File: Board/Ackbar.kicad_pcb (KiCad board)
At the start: 2 copper layers, 101.6 x 50.8 mm, 15 parts, among them J1 TOF, J2 GNSS, J3 HALL, J4 MOTOR, J5 PWR_IN, J6 EPD, U1 ESP32-S3 Pico, U2 VREG, U3 TMC2209, U4 SN74LVC1G04

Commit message: Add pullup resistor to vreg enable
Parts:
- added R2: 1K, Resistor_SMD:R_0805_2012Metric_Pad1.20x1.40mm_HandSolder, F.Cu at (101.6, 53.6)
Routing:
- net /VIN: track 57.0 -> 64.2 mm
- net Net-(U2-EN): track 23.2 -> 30.2 mm
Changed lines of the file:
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@@
+    )
+  )
+  (footprint "Resistor_SMD:R_0805_2012Metric_Pad1.20x1.40mm_HandSolder" (layer "F.Cu")
+    (at 101.6 53.61 -90)
+    (descr "Resistor SMD 0805 (2012 Metric), square (rectangular) end terminal, IPC_7351 nominal with elongated pad for handsoldering. (Body size source: IPC-SM-782 page 72, https://www.pcb-3d.com/wordpress/wp-content/uploads/ipc-sm-782a_amendment_1_and_2.pdf), generated with kicad-footprint-generator")
+    (tags "resistor handsolder")
+    (property "Sheetfile" "Ackbar.kicad_sch")
+    (property "Sheetname" "")
+    (property "ki_description" "Resistor, US symbol")
+    (property "ki_keywords" "R res resistor")
+    (attr smd)
+    (fp_text reference "R2" (at 0 -1.65 90) (layer "F.SilkS")
+        (effects (font (size 1 1) (thickness 0.15)))
+    )
+    (fp_text value "1K" (at 0 1.65 90) (layer "F.Fab")
+        (effects (font (size 1 1) (thickness 0.15)))
+    )
+    (fp_text user "${REFERENCE}" (at 0 0 90) (layer "F.Fab")
+        (effects (font (size 0.5 0.5) (thickness 0.08)))
+    )
+    (fp_line (start -0.227064 -0.735) (end 0.227064 -0.735)
+      (stroke (width 0.12) (type solid)) (layer "F.SilkS"))
+    (fp_line (start -0.227064 0.735) (end 0.227064 0.735)
+      (stroke (width 0.12) (type solid)) (layer "F.SilkS"))
+    (fp_line (start -1.85 -0.95) (end 1.85 -0.95)
+      (stroke (width 0.05) (type solid)) (layer "F.CrtYd"))
+    (fp_line (start -1.85 0.95) (end -1.85 -0.95)
+      (stroke (width 0.05) (type solid)) (layer "F.CrtYd"))
+    (fp_line (start 1.85 -0.95) (end 1.85 0.95)
+      (stroke (width 0.05) (type solid)) (layer "F.CrtYd"))
+    (fp_line (start 1.85 0.95) (end -1.85 0.95)
+      (stroke (width 0.05) (type solid)) (layer "F.CrtYd"))
+    (fp_line (start -1 -0.625) (end 1 -0.625)
+      (stroke (width 0.1) (type solid)) (layer "F.Fab"))
+    (fp_line (start -1 0.625) (end -1 -0.625)
+      (stroke (width 0.1) (type solid)) (layer "F.Fab"))
+    (fp_line (start 1 -0.625) (end 1 0.625)
+      (stroke (width 0.1) (type solid)) (layer "F.Fab"))
+    (fp_line (start 1 0.625) (end -1 0.625)
+      (stroke (width 0.1) (type solid)) (layer "F.Fab"))
+    (pad "1" smd roundrect (at -1 0 270) (size 1.2 1.4) (layers "F.Cu" "F.Paste" "F.Mask") (roundrect_rratio 0.208333)
+      (net 11 "/VIN") (pintype "passive"))
+    (pad "2" smd roundrect (at 1 0 270) (size 1.2 1.4) (layers "F.Cu" "F.Paste" "F.Mask") (roundrect_rratio 0.208333)
+      (net 41 "Net-(U2-EN)") (pintype "passive"))
+    (model "${KICAD6_3DMODEL_DIR}/Resistor_SMD.3dshapes/R_0805_2012Metric.wrl"
+      (offset (xyz 0 0 0))
+      (scale (xyz 1 1 1))
+      (rotate (xyz 0 0 0))
     )
   )
@@
   (segment (start 69.85 52.385) (end 67.625 52.385) (width 0.5) (layer "F.Cu") (net 9))
   (via (at 67.31 52.07) (size 0.8) (drill 0.4) (layers "F.Cu" "B.Cu") (net 9))
+  (segment (start 101.6 52.61) (end 98.965 52.61) (width 0.5) (layer "F.Cu") (net 11))
+  (segment (start 98.425 52.07) (end 94.615 52.07) (width 0.5) (layer "F.Cu") (net 11))
+  (segment (start 98.965 52.61) (end 98.425 52.07) (width 0.5) (layer "F.Cu") (net 11))
   (segment (start 100.965 49.53) (end 100.965 43.815) (width 0.5) (layer "B.Cu") (net 11))
   (segment (start 76.878 29.253) (end 76.878 27.224334) (width 0.5) (layer "B.Cu") (net 11))
@@
   (segment (start 87.038 27.224334) (end 87.038 17.188) (width 0.5) (layer "B.Cu") (net 39))
   (segment (start 89.578 27.224334) (end 89.578 17.188) (width 0.5) (layer "B.Cu") (net 40))
+  (segment (start 94.615 54.61) (end 101.6 54.61) (width 0.25) (layer "F.Cu") (net 41))
   (segment (start 74.585 54.61) (end 94.615 54.61) (width 0.25) (layer "F.Cu") (net 41))
   (segment (start 72.36 52.385) (end 74.585 54.61) (width 0.25) (layer "F.Cu") (net 41))

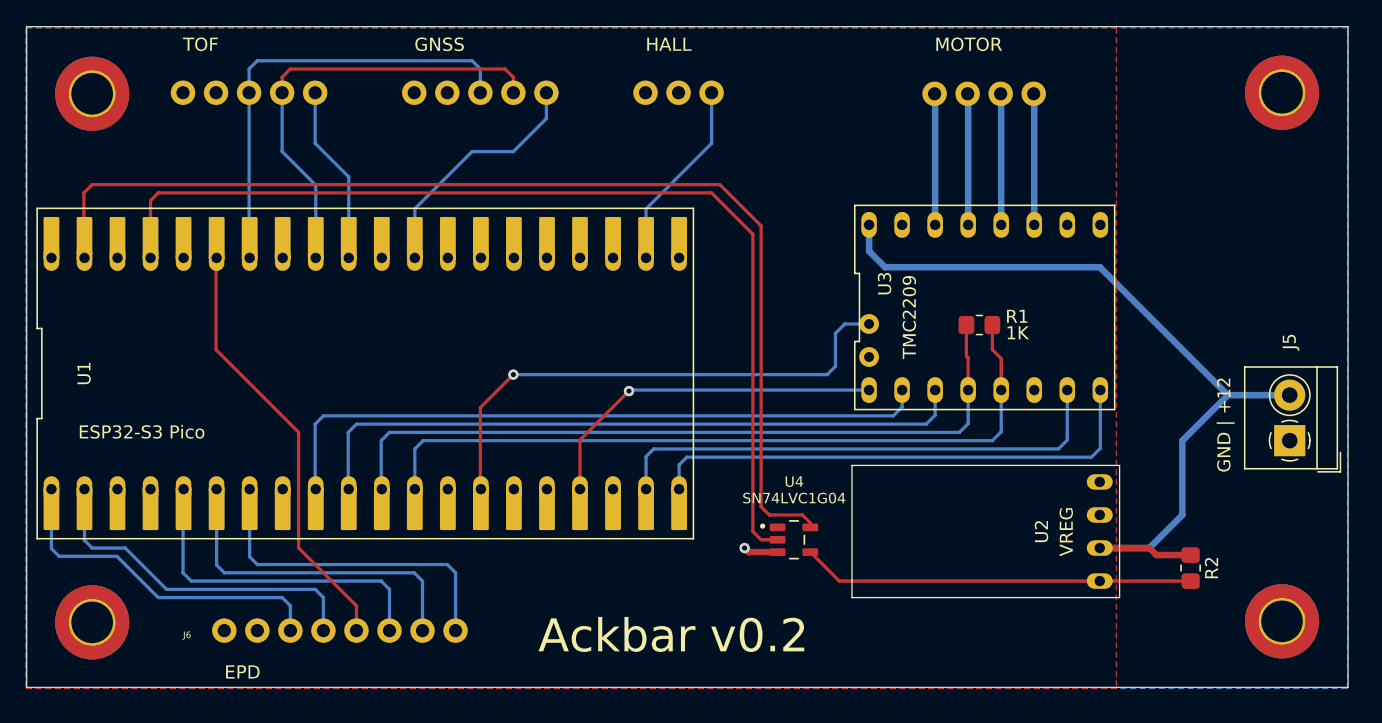
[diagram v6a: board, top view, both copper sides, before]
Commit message: Okay, you win, we're using the onboard regulator
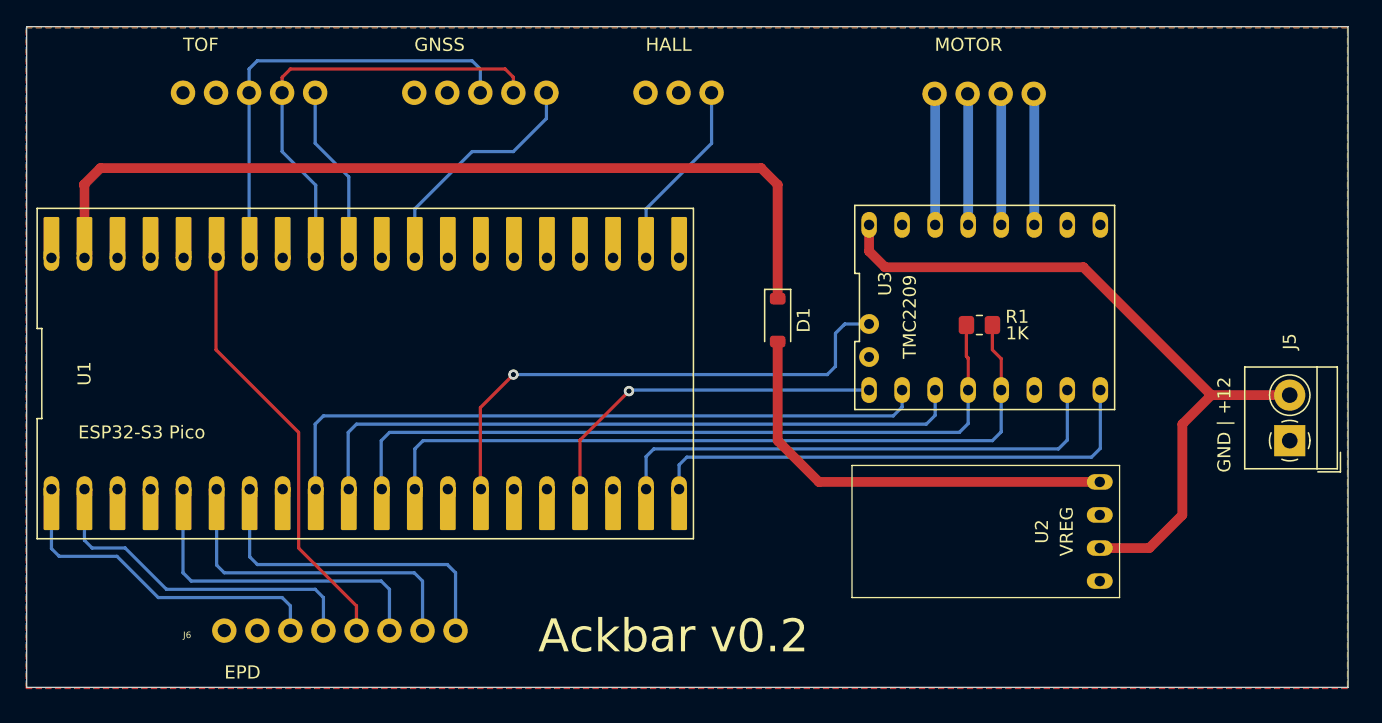
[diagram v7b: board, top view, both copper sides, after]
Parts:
- removed R2: 1K, Resistor_SMD:R_0805_2012Metric_Pad1.20x1.40mm_HandSolder
- removed REF** (x4): MountingHole_3.2mm_M3_ISO7380_Pad_TopBottom, MountingHole:MountingHole_3.2mm_M3_ISO7380_Pad_TopBottom
- removed U4: SN74LVC1G04, Ackbar:SOT95P280X145-5N
- added D1: MBR230LSFT1G, Diode_SMD:D_SOD-123, F.Cu at (69.8, 34.5)
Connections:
- U1 pad 37: Net-(U1-3V3_EN) -> unconnected-(U1-3V3_EN-Pad37)
- U1 pad 39: Net-(U1-VSYS) -> /VSYS
- U2 pad 1: /3V3 -> /VOUT
- U2 pad 4: Net-(U2-EN) -> unconnected-(U2-EN-Pad4)
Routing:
- net Net-(U1-VSYS): track 84.8 -> 0.00 mm
- net Net-(U1-3V3_EN): track 77.3 -> 0.00 mm
- net /VSYS: track 0.00 -> 68.8 mm
- net /VOUT: track 0.00 -> 33.7 mm
- net Net-(U2-EN): track 30.2 -> 0.00 mm
- net /VIN: track 64.2 -> 56.5 mm
- net /GND: track 2.67 -> 0.00 mm, vias 1 -> 0

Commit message: Replace missing mounting holes
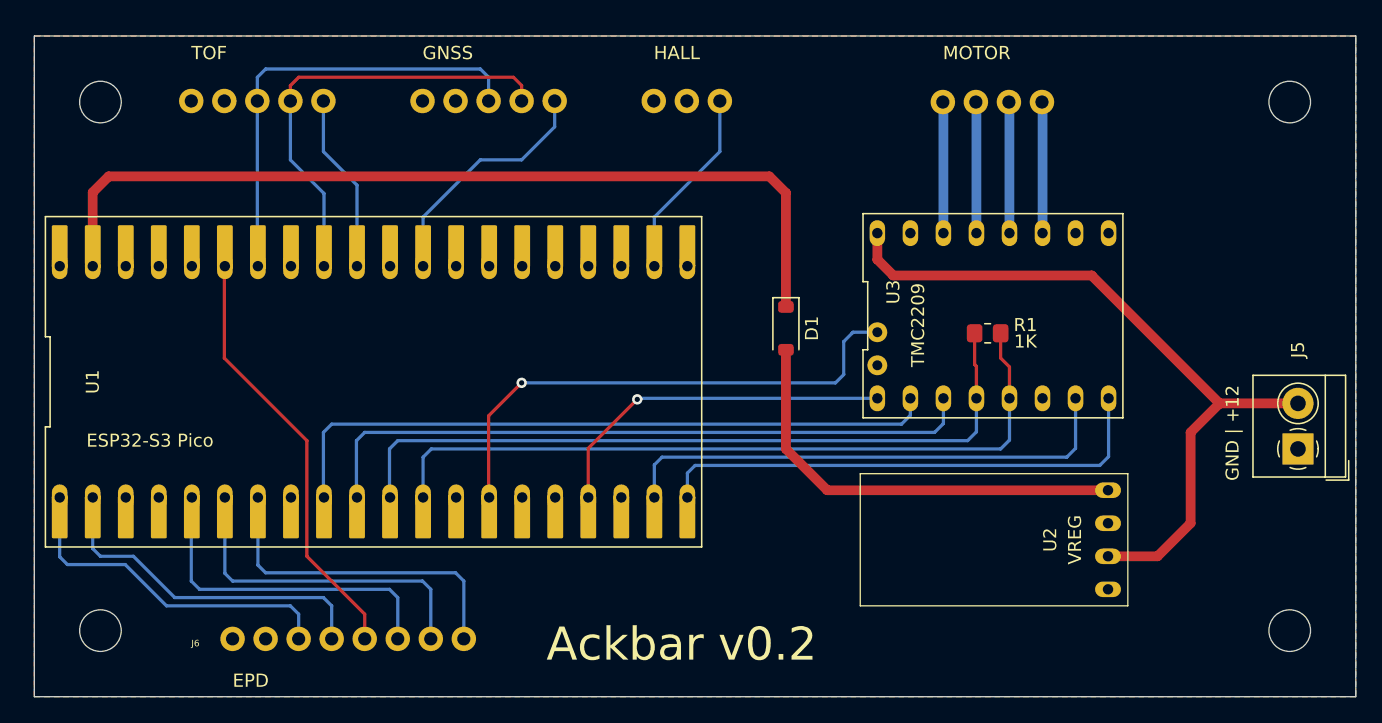
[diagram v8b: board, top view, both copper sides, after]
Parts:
- added H1: MountingHole, MountingHole:MountingHole_3.2mm_M3, F.Cu at (17.8, 17.8)
- added H2: MountingHole, MountingHole:MountingHole_3.2mm_M3, F.Cu at (109.2, 17.8)
- added H3: MountingHole, MountingHole:MountingHole_3.2mm_M3, F.Cu at (17.8, 58.4)
- added H4: MountingHole, MountingHole:MountingHole_3.2mm_M3, F.Cu at (109.2, 58.4)
- moved J5 0.90 mm to (109.9, 44.5)
- moved R1 0.90 mm to (86.0, 35.6)
- moved U2 0.90 mm to (95.2, 51.4)
- moved J2 0.90 mm to (42.5, 17.7)
- moved J3 0.90 mm to (60.3, 17.7)
- moved J1 0.90 mm to (24.8, 17.7)
- moved D1 0.90 mm to (70.5, 35.2)
- moved U3 0.90 mm to (86.4, 34.2)
- moved J6 0.90 mm to (27.9, 59.1)
- moved U1 0.90 mm to (38.8, 39.3)
- moved J4 0.90 mm to (82.5, 17.8)
